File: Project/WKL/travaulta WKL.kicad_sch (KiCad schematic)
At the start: 27 parts, among them J5 ARGB, SW38 BOOT0, U1 STM32F401CBUx, U2 XC6206PxxxMR, Y1 8 MHz

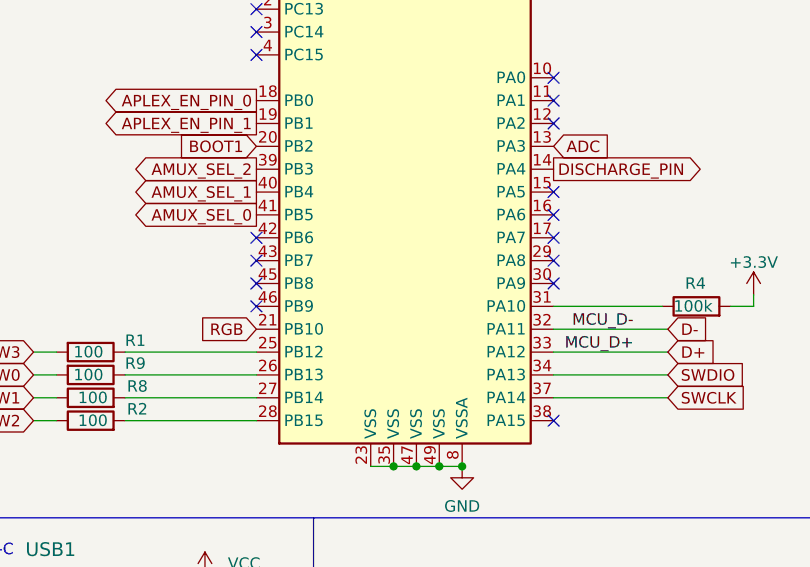
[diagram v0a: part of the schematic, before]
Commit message: changed rgb pin on HHKB&WKL for better compatibility
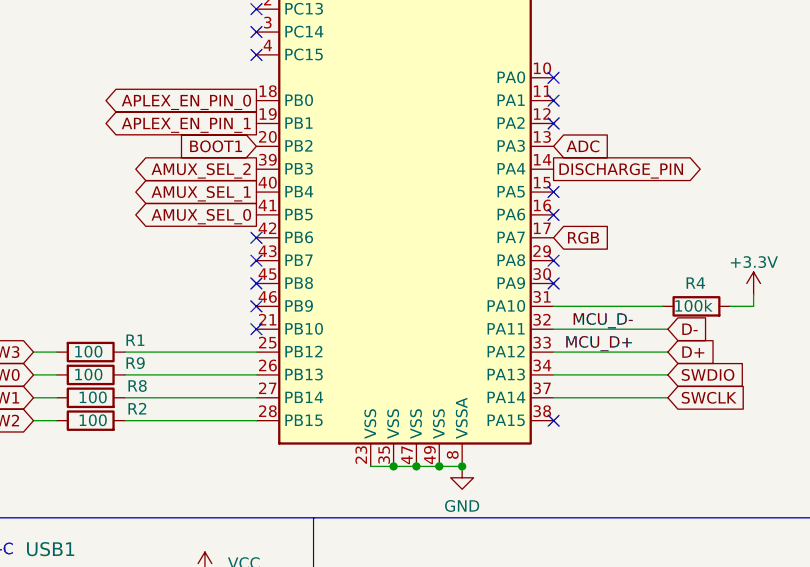
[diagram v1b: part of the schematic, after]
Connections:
- net RGB: now also U1.17 (PA7); no longer U1.21 (PB10)
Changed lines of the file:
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@@
   (no_connect (at 46.355 81.28))
   (no_connect (at 79.375 81.28))
-  (no_connect (at 79.375 76.2))
+  (no_connect (at 46.355 86.36))
   (no_connect (at 46.355 83.82))
   (no_connect (at 79.375 71.12))
@@
     )
   )
-  (global_label "RGB" (shape input) (at 46.355 86.36 180) (fields_autoplaced)
-    (effects (font (size 1.27 1.27)) (justify right))
-    (property "Intersheetrefs" "${INTERSHEET_REFS}" (at 39.6392 86.36 0)
-      (effects (font (size 1.27 1.27)) (justify right) hide)
-    )
-  )
+  (global_label "RGB" (shape input) (at 79.375 76.2 0) (fields_autoplaced)
+    (effects (font (size 1.27 1.27)) (justify left))
+    (property "Intersheetrefs" "${INTERSHEET_REFS}" (at 86.0908 76.2 0)
+      (effects (font (size 1.27 1.27)) (justify left) hide)
+    )
+  )
